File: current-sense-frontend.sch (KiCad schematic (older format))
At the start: 8 parts

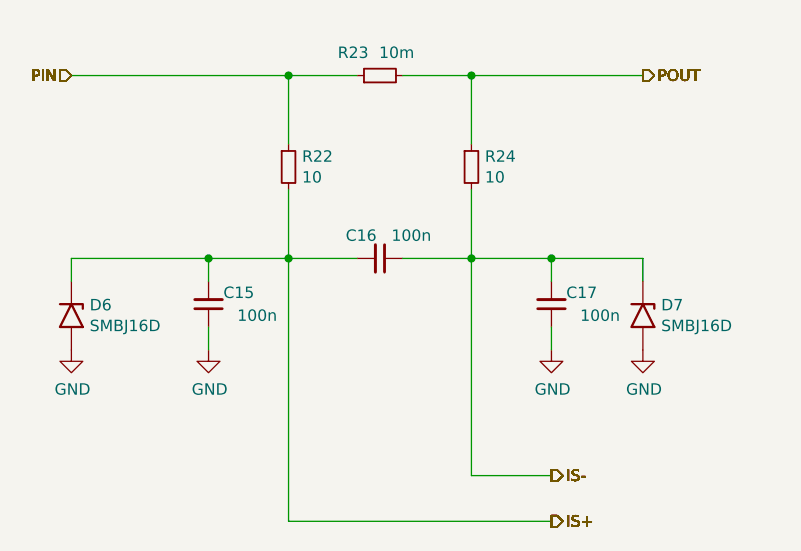
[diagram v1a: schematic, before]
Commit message: Add fiducials, fix aesthetics in schematics
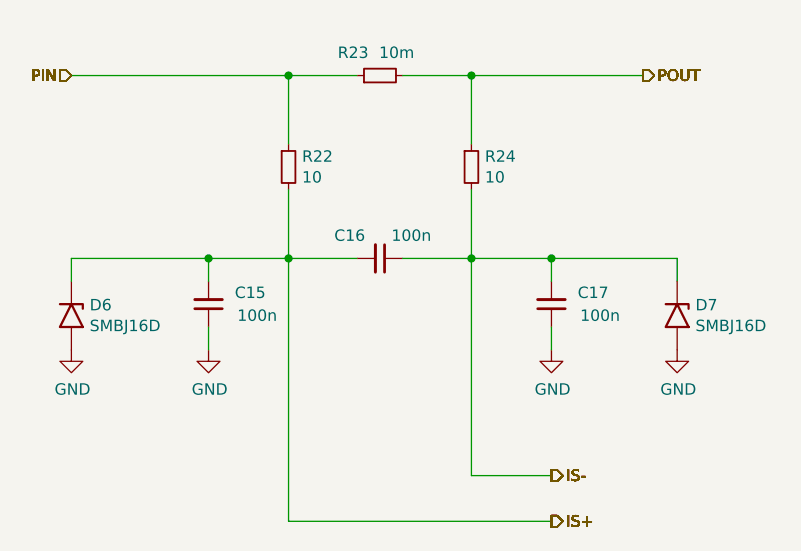
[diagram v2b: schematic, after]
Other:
- moved on the sheet: D7
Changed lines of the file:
@@
 encoding utf-8
 Sheet 4 6
-Title ""
+Title "Tougher INA3221 Power Meter"
 Date ""
 Rev ""
-Comp ""
+Comp "Beast Devices"
 Comment1 ""
 Comment2 ""
@@
 Connection ~ 6050 2450
 Wire Wire Line
-	6400 2450 6800 2450
-Wire Wire Line
-	6800 2450 6800 2550
-Connection ~ 6400 2450
+	6400 2450 6950 2450
+Wire Wire Line
+	6950 2450 6950 2550
 Wire Wire Line
 	4900 2750 4900 2850
@@
 AR Path="/5F4101BA/5F4111AD" Ref="C13"  Part="1"
 AR Path="/5F404FBF/5F4111AD" Ref="C16"  Part="1"
-F 0 "C16" V 5550 2300 50  0000 L CNN
+F 0 "C16" V 5550 2250 50  0000 L CNN
 F 1 "100n" V 5550 2500 50  0000 L CNN
 F 2 "Capacitor_SMD:C_0603_1608Metric" H 5650 2450 50  0001 C CNN
@@
 AR Path="/5F4101BA/5F41791D" Ref="C14"  Part="1"
 AR Path="/5F404FBF/5F41791D" Ref="C17"  Part="1"
-F 0 "C17" H 6200 2600 50  0000 L CNN
+F 0 "C17" H 6150 2600 50  0000 L CNN
 F 1 "100n" H 6100 2700 50  0000 L CNN
 F 2 "Capacitor_SMD:C_0603_1608Metric" H 6400 2650 50  0001 C CNN
@@
 AR Path="/5F4101BA/5F41791C" Ref="C12"  Part="1"
 AR Path="/5F404FBF/5F41791C" Ref="C15"  Part="1"
-F 0 "C15" H 4700 2600 50  0000 L CNN
+F 0 "C15" H 4650 2600 50  0000 L CNN
 F 1 "100n" H 4600 2700 50  0000 L CNN
 F 2 "Capacitor_SMD:C_0603_1608Metric" H 4900 2650 50  0001 C CNN
@@
 L Diodes:SMBJxxxD D3
 U 1 1 5F417918
-P 6800 2700
+P 6950 2700
 AR Path="/5F41030B/5F417918" Ref="D3"  Part="1"
 AR Path="/5F4101BA/5F417918" Ref="D5"  Part="1"
 AR Path="/5F404FBF/5F417918" Ref="D7"  Part="1"
-F 0 "D7" V 6754 2780 50  0000 L CNN
-F 1 "SMBJ16D" V 6845 2780 50  0000 L CNN
-F 2 "Diode_SMD:D_SMB" H 6800 2500 50  0001 C CNN
-F 3 "https://www.vishay.com/docs/87606/smbj5cdthrusmbj120cd.pdf" H 6750 2700 50  0001 C CNN
-	1    6800 2700
+F 0 "D7" V 6904 2780 50  0000 L CNN
+F 1 "SMBJ16D" V 6995 2780 50  0000 L CNN
+F 2 "Diode_SMD:D_SMB" H 6950 2500 50  0001 C CNN
+F 3 "https://www.vishay.com/docs/87606/smbj5cdthrusmbj120cd.pdf" H 6900 2700 50  0001 C CNN
+	1    6950 2700
 	0    1    1    0
 $EndComp
@@
 L power:GND #PWR043
 U 1 1 5F548ADA
-P 6800 2850
+P 6950 2850
 AR Path="/5F404FBF/5F548ADA" Ref="#PWR043"  Part="1"
 AR Path="/5F41030B/5F548ADA" Ref="#PWR035"  Part="1"
 AR Path="/5F4101BA/5F548ADA" Ref="#PWR039"  Part="1"
-F 0 "#PWR043" H 6800 2600 50  0001 C CNN
-F 1 "GND" H 6805 2677 50  0000 C CNN
-F 2 "" H 6800 2850 50  0001 C CNN
-F 3 "" H 6800 2850 50  0001 C CNN
-	1    6800 2850
-	1    0    0    -1
-$EndComp
+F 0 "#PWR043" H 6950 2600 50  0001 C CNN
+F 1 "GND" H 6955 2677 50  0000 C CNN
+F 2 "" H 6950 2850 50  0001 C CNN
+F 3 "" H 6950 2850 50  0001 C CNN
+	1    6950 2850
+	1    0    0    -1
+$EndComp
+Connection ~ 6400 2450
 $EndSCHEMATC

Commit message: Add manufacturers, part numbers, and supplier links
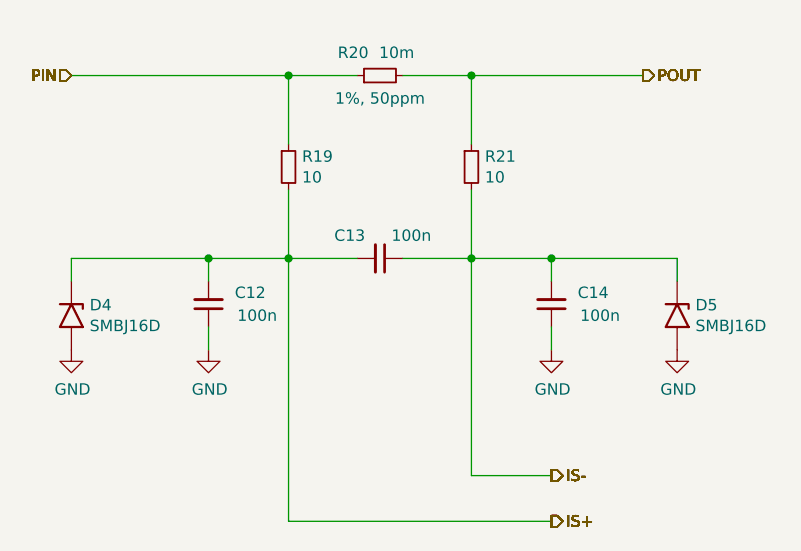
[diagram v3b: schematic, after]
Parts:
- C10, C11, C9: Voltage (none) -> 50V
- D2, D3: Distributor Link (none) -> https://www.digikey.se/product-detail/en/vishay-semiconduct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; Manufacturer (none) -> Vishay Semiconductor Diodes Division; Part Number (none) -> SMBJ16D-M3/I
- R16, R18: Tolerance (none) -> 1%
- R17: Distributor Link (none) -> https://www.digikey.se/product-detail/en/yageo/PE2512FKE070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; Manufacturer (none) -> Yageo; Part Number (none) -> PE2512FKE070R01L; Tolerance (none) -> 1%, 50ppm
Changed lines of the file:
@@
 $Descr A4 11693 8268
 encoding utf-8
-Sheet 4 6
+Sheet 3 6
 Title "Tougher INA3221 Power Meter"
 Date ""
@@
 AR Path="/5F4101BA/5F4111AC" Ref="R20"  Part="1"
 AR Path="/5F404FBF/5F4111AC" Ref="R23"  Part="1"
-F 0 "R23" V 5750 1700 50  0000 L CNN
+F 0 "R20" V 5750 1700 50  0000 L CNN
 F 1 "10m" V 5750 1500 50  0000 L CNN
 F 2 "Resistor_SMD:R_2512_6332Metric" H 5650 1650 50  0001 C CNN
 F 3 "~" H 5650 1650 50  0001 C CNN
+F 4 "https://www.digikey.se/product-detail/en/yageo/PE2512FKE070R01L/YAG2151CT-ND/5139599" H 5650 1650 50  0001 C CNN "Distributor Link"
+F 5 "Yageo" H 5650 1650 50  0001 C CNN "Manufacturer"
+F 6 "PE2512FKE070R01L" H 5650 1650 50  0001 C CNN "Part Number"
+F 7 "1%, 50ppm" V 5550 1650 50  0000 C CNN "Tolerance"
 	1    5650 1650
 	0    -1   -1   0
@@
 AR Path="/5F4101BA/5F4111AD" Ref="C13"  Part="1"
 AR Path="/5F404FBF/5F4111AD" Ref="C16"  Part="1"
-F 0 "C16" V 5550 2250 50  0000 L CNN
+F 0 "C13" V 5550 2250 50  0000 L CNN
 F 1 "100n" V 5550 2500 50  0000 L CNN
 F 2 "Capacitor_SMD:C_0603_1608Metric" H 5650 2450 50  0001 C CNN
 F 3 "~" H 5650 2450 50  0001 C CNN
+F 4 "50V" H 5650 2450 50  0001 C CNN "Voltage"
 	1    5650 2450
 	0    1    1    0
@@
 AR Path="/5F4101BA/5F4111AE" Ref="R19"  Part="1"
 AR Path="/5F404FBF/5F4111AE" Ref="R22"  Part="1"
-F 0 "R22" H 5309 2096 50  0000 L CNN
+F 0 "R19" H 5309 2096 50  0000 L CNN
 F 1 "10" H 5309 2005 50  0000 L CNN
 F 2 "Resistor_SMD:R_0603_1608Metric" H 5250 2050 50  0001 C CNN
 F 3 "~" H 5250 2050 50  0001 C CNN
+F 4 "1%" H 5250 2050 50  0001 C CNN "Tolerance"
 	1    5250 2050
 	1    0    0    -1
@@
 AR Path="/5F4101BA/5F41791D" Ref="C14"  Part="1"
 AR Path="/5F404FBF/5F41791D" Ref="C17"  Part="1"
-F 0 "C17" H 6150 2600 50  0000 L CNN
+F 0 "C14" H 6150 2600 50  0000 L CNN
 F 1 "100n" H 6100 2700 50  0000 L CNN
 F 2 "Capacitor_SMD:C_0603_1608Metric" H 6400 2650 50  0001 C CNN
 F 3 "~" H 6400 2650 50  0001 C CNN
+F 4 "50V" H 6400 2650 50  0001 C CNN "Voltage"
 	1    6400 2650
 	-1   0    0    1
@@
 AR Path="/5F4101BA/5F41791E" Ref="R21"  Part="1"
 AR Path="/5F404FBF/5F41791E" Ref="R24"  Part="1"
-F 0 "R24" H 6109 2096 50  0000 L CNN
+F 0 "R21" H 6109 2096 50  0000 L CNN
 F 1 "10" H 6109 2005 50  0000 L CNN
 F 2 "Resistor_SMD:R_0603_1608Metric" H 6050 2050 50  0001 C CNN
 F 3 "~" H 6050 2050 50  0001 C CNN
+F 4 "1%" H 6050 2050 50  0001 C CNN "Tolerance"
 	1    6050 2050
 	1    0    0    -1
@@
 AR Path="/5F4101BA/5F41791C" Ref="C12"  Part="1"
 AR Path="/5F404FBF/5F41791C" Ref="C15"  Part="1"
-F 0 "C15" H 4650 2600 50  0000 L CNN
+F 0 "C12" H 4650 2600 50  0000 L CNN
 F 1 "100n" H 4600 2700 50  0000 L CNN
 F 2 "Capacitor_SMD:C_0603_1608Metric" H 4900 2650 50  0001 C CNN
 F 3 "~" H 4900 2650 50  0001 C CNN
+F 4 "50V" H 4900 2650 50  0001 C CNN "Voltage"
 	1    4900 2650
 	-1   0    0    1
@@
 AR Path="/5F4101BA/5F41791A" Ref="D4"  Part="1"
 AR Path="/5F404FBF/5F41791A" Ref="D6"  Part="1"
-F 0 "D6" V 4254 2780 50  0000 L CNN
+F 0 "D4" V 4254 2780 50  0000 L CNN
 F 1 "SMBJ16D" V 4345 2780 50  0000 L CNN
 F 2 "Diode_SMD:D_SMB" H 4300 2500 50  0001 C CNN
 F 3 "https://www.vishay.com/docs/87606/smbj5cdthrusmbj120cd.pdf" H 4250 2700 50  0001 C CNN
+F 4 "https://www.digikey.se/product-detail/en/vishay-semiconductor-diodes-division/SMBJ16D-M3-I/SMBJ16D-M3-IGICT-ND/9648416" H 4300 2700 50  0001 C CNN "Distributor Link"
+F 5 "Vishay Semiconductor Diodes Division" H 4300 2700 50  0001 C CNN "Manufacturer"
+F 6 "SMBJ16D-M3/I" H 4300 2700 50  0001 C CNN "Part Number"
 	1    4300 2700
 	0    1    1    0
@@
 AR Path="/5F4101BA/5F417918" Ref="D5"  Part="1"
 AR Path="/5F404FBF/5F417918" Ref="D7"  Part="1"
-F 0 "D7" V 6904 2780 50  0000 L CNN
+F 0 "D5" V 6904 2780 50  0000 L CNN
 F 1 "SMBJ16D" V 6995 2780 50  0000 L CNN
 F 2 "Diode_SMD:D_SMB" H 6950 2500 50  0001 C CNN
 F 3 "https://www.vishay.com/docs/87606/smbj5cdthrusmbj120cd.pdf" H 6900 2700 50  0001 C CNN
+F 4 "https://www.digikey.se/product-detail/en/vishay-semiconductor-diodes-division/SMBJ16D-M3-I/SMBJ16D-M3-IGICT-ND/9648416" H 6950 2700 50  0001 C CNN "Distributor Link"
+F 5 "Vishay Semiconductor Diodes Division" H 6950 2700 50  0001 C CNN "Manufacturer"
+F 6 "SMBJ16D-M3/I" H 6950 2700 50  0001 C CNN "Part Number"
 	1    6950 2700
 	0    1    1    0
@@
 AR Path="/5F41030B/5F54837F" Ref="#PWR032"  Part="1"
 AR Path="/5F4101BA/5F54837F" Ref="#PWR036"  Part="1"
-F 0 "#PWR040" H 4300 2600 50  0001 C CNN
+F 0 "#PWR036" H 4300 2600 50  0001 C CNN
 F 1 "GND" H 4305 2677 50  0000 C CNN
 F 2 "" H 4300 2850 50  0001 C CNN
@@
 AR Path="/5F41030B/5F5484AE" Ref="#PWR033"  Part="1"
 AR Path="/5F4101BA/5F5484AE" Ref="#PWR037"  Part="1"
-F 0 "#PWR041" H 4900 2600 50  0001 C CNN
+F 0 "#PWR037" H 4900 2600 50  0001 C CNN
 F 1 "GND" H 4905 2677 50  0000 C CNN
 F 2 "" H 4900 2850 50  0001 C CNN
@@
 AR Path="/5F41030B/5F54854F" Ref="#PWR034"  Part="1"
 AR Path="/5F4101BA/5F54854F" Ref="#PWR038"  Part="1"
-F 0 "#PWR042" H 6400 2600 50  0001 C CNN
+F 0 "#PWR038" H 6400 2600 50  0001 C CNN
 F 1 "GND" H 6405 2677 50  0000 C CNN
 F 2 "" H 6400 2850 50  0001 C CNN
@@
 AR Path="/5F41030B/5F548ADA" Ref="#PWR035"  Part="1"
 AR Path="/5F4101BA/5F548ADA" Ref="#PWR039"  Part="1"
-F 0 "#PWR043" H 6950 2600 50  0001 C CNN
+F 0 "#PWR039" H 6950 2600 50  0001 C CNN
 F 1 "GND" H 6955 2677 50  0000 C CNN
 F 2 "" H 6950 2850 50  0001 C CNN

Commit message: Change part number for the current sense resistor
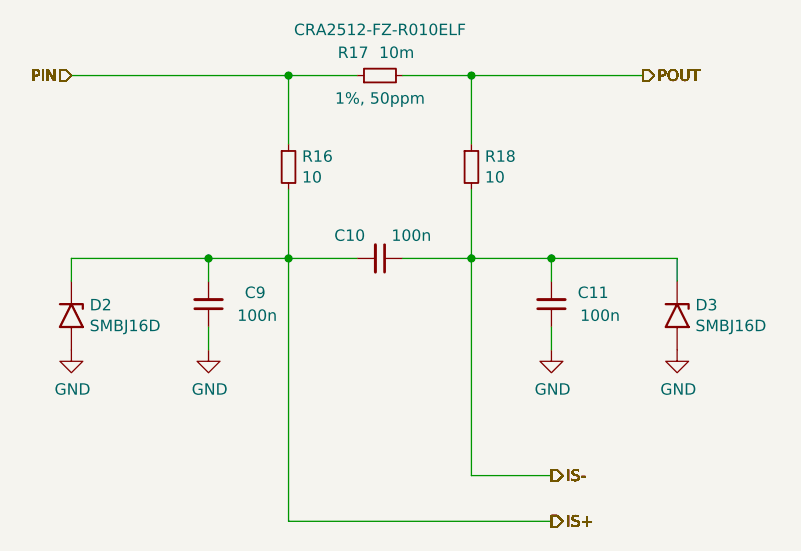
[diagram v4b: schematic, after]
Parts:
- R17: Distributor Link https://www.digikey.se/product-detail/en/yageo/PE2512FKE070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 -> https://www.digikey.se/product-detail/en/CRA2512-FZ-R010ELF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; Manufacturer Yageo -> Bourns; Part Number PE2512FKE070R01L -> CRA2512-FZ-R010ELF
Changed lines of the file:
@@
 $Descr A4 11693 8268
 encoding utf-8
-Sheet 3 6
+Sheet 2 6
 Title "Tougher INA3221 Power Meter"
 Date ""
@@
 AR Path="/5F4101BA/5F4111AC" Ref="R20"  Part="1"
 AR Path="/5F404FBF/5F4111AC" Ref="R23"  Part="1"
-F 0 "R20" V 5750 1700 50  0000 L CNN
+F 0 "R17" V 5750 1700 50  0000 L CNN
 F 1 "10m" V 5750 1500 50  0000 L CNN
 F 2 "Resistor_SMD:R_2512_6332Metric" H 5650 1650 50  0001 C CNN
-F 3 "~" H 5650 1650 50  0001 C CNN
-F 4 "https://www.digikey.se/product-detail/en/yageo/PE2512FKE070R01L/YAG2151CT-ND/5139599" H 5650 1650 50  0001 C CNN "Distributor Link"
-F 5 "Yageo" H 5650 1650 50  0001 C CNN "Manufacturer"
-F 6 "PE2512FKE070R01L" H 5650 1650 50  0001 C CNN "Part Number"
+F 3 "https://www.bourns.com/docs/product-datasheets/cra.pdf" H 5650 1650 50  0001 C CNN
+F 4 "https://www.digikey.se/product-detail/en/CRA2512-FZ-R010ELF/CRA2512-FZ-R010ELFCT-ND/1775054/?itemSeq=339344556" H 5650 1650 50  0001 C CNN "Distributor Link"
+F 5 "Bourns" H 5650 1650 50  0001 C CNN "Manufacturer"
+F 6 "CRA2512-FZ-R010ELF" V 5850 1650 50  0000 C CNN "Part Number"
 F 7 "1%, 50ppm" V 5550 1650 50  0000 C CNN "Tolerance"
 	1    5650 1650
@@
 AR Path="/5F4101BA/5F4111AD" Ref="C13"  Part="1"
 AR Path="/5F404FBF/5F4111AD" Ref="C16"  Part="1"
-F 0 "C13" V 5550 2250 50  0000 L CNN
+F 0 "C10" V 5550 2250 50  0000 L CNN
 F 1 "100n" V 5550 2500 50  0000 L CNN
 F 2 "Capacitor_SMD:C_0603_1608Metric" H 5650 2450 50  0001 C CNN
@@
 AR Path="/5F4101BA/5F4111AE" Ref="R19"  Part="1"
 AR Path="/5F404FBF/5F4111AE" Ref="R22"  Part="1"
-F 0 "R19" H 5309 2096 50  0000 L CNN
+F 0 "R16" H 5309 2096 50  0000 L CNN
 F 1 "10" H 5309 2005 50  0000 L CNN
 F 2 "Resistor_SMD:R_0603_1608Metric" H 5250 2050 50  0001 C CNN
@@
 AR Path="/5F4101BA/5F41791D" Ref="C14"  Part="1"
 AR Path="/5F404FBF/5F41791D" Ref="C17"  Part="1"
-F 0 "C14" H 6150 2600 50  0000 L CNN
+F 0 "C11" H 6150 2600 50  0000 L CNN
 F 1 "100n" H 6100 2700 50  0000 L CNN
 F 2 "Capacitor_SMD:C_0603_1608Metric" H 6400 2650 50  0001 C CNN
@@
 AR Path="/5F4101BA/5F41791E" Ref="R21"  Part="1"
 AR Path="/5F404FBF/5F41791E" Ref="R24"  Part="1"
-F 0 "R21" H 6109 2096 50  0000 L CNN
+F 0 "R18" H 6109 2096 50  0000 L CNN
 F 1 "10" H 6109 2005 50  0000 L CNN
 F 2 "Resistor_SMD:R_0603_1608Metric" H 6050 2050 50  0001 C CNN
@@
 AR Path="/5F4101BA/5F41791C" Ref="C12"  Part="1"
 AR Path="/5F404FBF/5F41791C" Ref="C15"  Part="1"
-F 0 "C12" H 4650 2600 50  0000 L CNN
+F 0 "C9" H 4650 2600 50  0000 L CNN
 F 1 "100n" H 4600 2700 50  0000 L CNN
 F 2 "Capacitor_SMD:C_0603_1608Metric" H 4900 2650 50  0001 C CNN
@@
 AR Path="/5F4101BA/5F41791A" Ref="D4"  Part="1"
 AR Path="/5F404FBF/5F41791A" Ref="D6"  Part="1"
-F 0 "D4" V 4254 2780 50  0000 L CNN
+F 0 "D2" V 4254 2780 50  0000 L CNN
 F 1 "SMBJ16D" V 4345 2780 50  0000 L CNN
 F 2 "Diode_SMD:D_SMB" H 4300 2500 50  0001 C CNN
@@
 AR Path="/5F4101BA/5F417918" Ref="D5"  Part="1"
 AR Path="/5F404FBF/5F417918" Ref="D7"  Part="1"
-F 0 "D5" V 6904 2780 50  0000 L CNN
+F 0 "D3" V 6904 2780 50  0000 L CNN
 F 1 "SMBJ16D" V 6995 2780 50  0000 L CNN
 F 2 "Diode_SMD:D_SMB" H 6950 2500 50  0001 C CNN
@@
 AR Path="/5F41030B/5F54837F" Ref="#PWR032"  Part="1"
 AR Path="/5F4101BA/5F54837F" Ref="#PWR036"  Part="1"
-F 0 "#PWR036" H 4300 2600 50  0001 C CNN
+F 0 "#PWR032" H 4300 2600 50  0001 C CNN
 F 1 "GND" H 4305 2677 50  0000 C CNN
 F 2 "" H 4300 2850 50  0001 C CNN
@@
 AR Path="/5F41030B/5F5484AE" Ref="#PWR033"  Part="1"
 AR Path="/5F4101BA/5F5484AE" Ref="#PWR037"  Part="1"
-F 0 "#PWR037" H 4900 2600 50  0001 C CNN
+F 0 "#PWR033" H 4900 2600 50  0001 C CNN
 F 1 "GND" H 4905 2677 50  0000 C CNN
 F 2 "" H 4900 2850 50  0001 C CNN
@@
 AR Path="/5F41030B/5F54854F" Ref="#PWR034"  Part="1"
 AR Path="/5F4101BA/5F54854F" Ref="#PWR038"  Part="1"
-F 0 "#PWR038" H 6400 2600 50  0001 C CNN
+F 0 "#PWR034" H 6400 2600 50  0001 C CNN
 F 1 "GND" H 6405 2677 50  0000 C CNN
 F 2 "" H 6400 2850 50  0001 C CNN
@@
 AR Path="/5F41030B/5F548ADA" Ref="#PWR035"  Part="1"
 AR Path="/5F4101BA/5F548ADA" Ref="#PWR039"  Part="1"
-F 0 "#PWR039" H 6950 2600 50  0001 C CNN
+F 0 "#PWR035" H 6950 2600 50  0001 C CNN
 F 1 "GND" H 6955 2677 50  0000 C CNN
 F 2 "" H 6950 2850 50  0001 C CNN

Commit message: Add submodule for the KiCad libraries.
Add submodule for the KiCad libraries and change
references to the libraries.
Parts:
- D2, D3: symbol Diodes:SMBJxxxD -> Diode_BD:SMBJxxxD
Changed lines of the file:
@@
 $EndComp
 $Comp
-L Diodes:SMBJxxxD D2
+L Diode_BD:SMBJxxxD D2
 U 1 1 5F41791A
 P 4300 2700
@@
 $EndComp
 $Comp
-L Diodes:SMBJxxxD D3
+L Diode_BD:SMBJxxxD D3
 U 1 1 5F417918
 P 6950 2700
